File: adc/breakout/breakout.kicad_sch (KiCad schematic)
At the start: 52 parts, among them J1 Conn_01x05_Pin, J2 Conn_01x05_Pin, J3 Conn_01x03_Pin, J4 Conn_01x06_Pin, U1 ESD5344D-TP, U2 ADS1261IRHBR, U3 ESD5344D-TP, U4 ESD5344D-TP

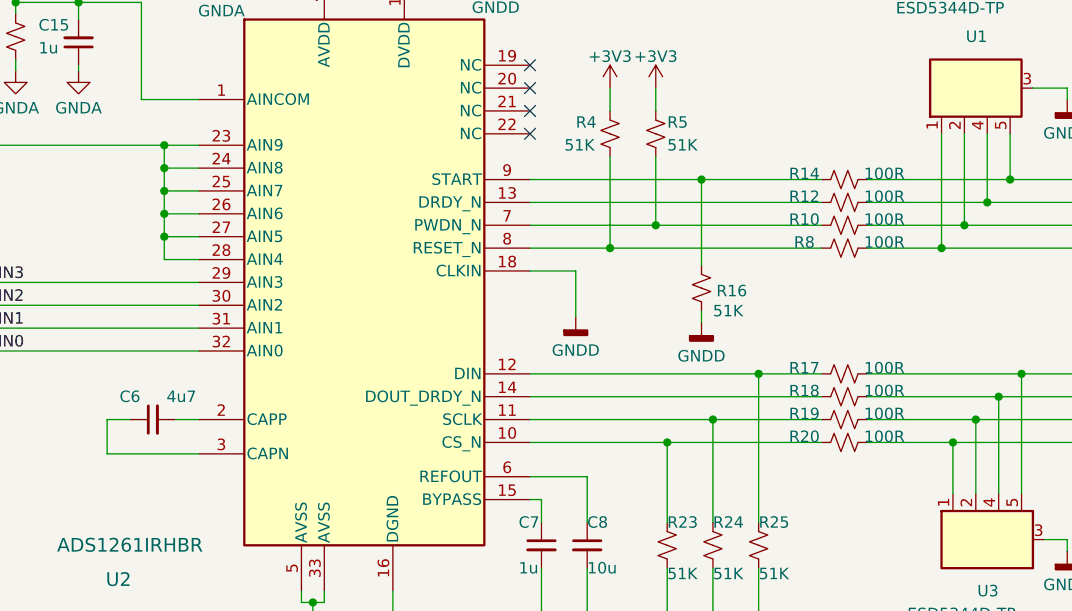
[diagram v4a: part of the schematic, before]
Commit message: Fixed two component values.
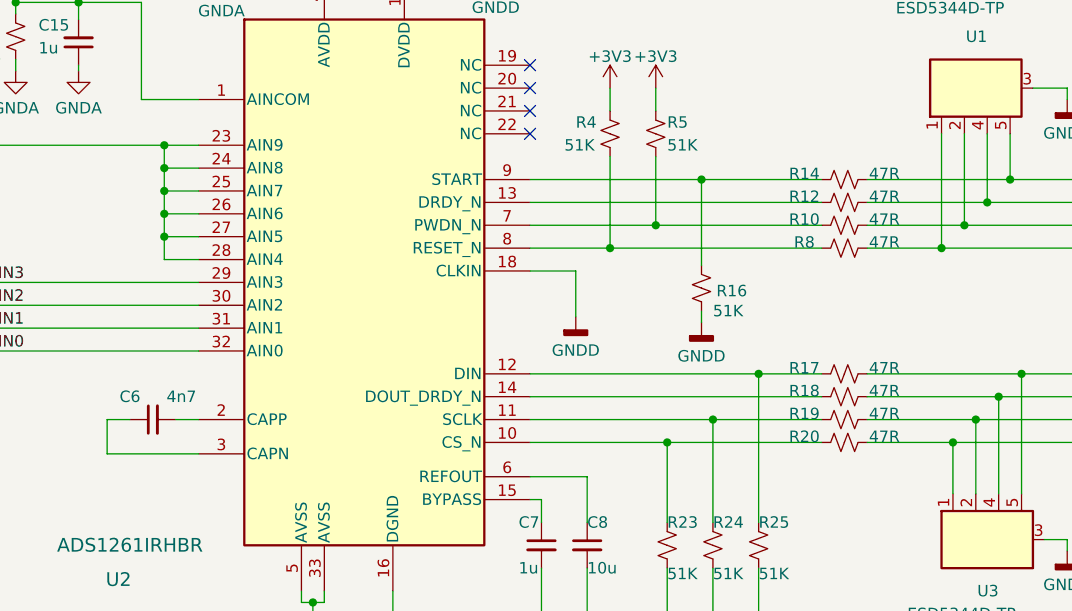
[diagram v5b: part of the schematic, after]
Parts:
- C6: value 4u7 -> 4n7; LCSC C23733 -> C1538
- R10, R12, R14, R17, R18, R19, R20, R8: value 100R -> 47R; LCSC C25076 -> C25118
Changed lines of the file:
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@@
       (effects (font (size 1.27 1.27)))
     )
-    (property "Value" "100R" (at 153.67 75.565 90)
+    (property "Value" "47R" (at 153.67 75.565 90)
       (effects (font (size 1.27 1.27)))
     )
@@
       (effects (font (size 1.27 1.27)) hide)
     )
-    (property "LCSC" "C25076" (at 149.225 76.2 0)
+    (property "LCSC" "C25118" (at 149.225 76.2 0)
       (effects (font (size 1.27 1.27)) hide)
     )
@@
       (effects (font (size 1.27 1.27)))
     )
-    (property "Value" "100R" (at 153.67 73.025 90)
+    (property "Value" "47R" (at 153.67 73.025 90)
       (effects (font (size 1.27 1.27)))
     )
@@
       (effects (font (size 1.27 1.27)) hide)
     )
-    (property "LCSC" "C25076" (at 149.225 73.66 0)
+    (property "LCSC" "C25118" (at 149.225 73.66 0)
       (effects (font (size 1.27 1.27)) hide)
     )
@@
       (effects (font (size 1.27 1.27)))
     )
-    (property "Value" "100R" (at 153.67 89.535 90)
+    (property "Value" "47R" (at 153.67 89.535 90)
       (effects (font (size 1.27 1.27)))
     )
@@
       (effects (font (size 1.27 1.27)) hide)
     )
-    (property "LCSC" "C25076" (at 149.225 90.17 0)
+    (property "LCSC" "C25118" (at 149.225 90.17 0)
       (effects (font (size 1.27 1.27)) hide)
     )
@@
       (effects (font (size 1.27 1.27)))
     )
-    (property "Value" "4u7" (at 75.565 92.71 90)
+    (property "Value" "4n7" (at 75.565 92.71 90)
       (effects (font (size 1.27 1.27)))
     )
@@
       (effects (font (size 1.27 1.27)) hide)
     )
-    (property "LCSC" "C23733" (at 72.39 95.25 0)
+    (property "LCSC" "C1538" (at 72.39 95.25 0)
       (effects (font (size 1.27 1.27)) hide)
     )
@@
       (effects (font (size 1.27 1.27)))
     )
-    (property "Value" "100R" (at 153.67 70.485 90)
+    (property "Value" "47R" (at 153.67 70.485 90)
       (effects (font (size 1.27 1.27)))
     )
@@
       (effects (font (size 1.27 1.27)) hide)
     )
-    (property "LCSC" "C25076" (at 149.225 71.12 0)
+    (property "LCSC" "C25118" (at 149.225 71.12 0)
       (effects (font (size 1.27 1.27)) hide)
     )
@@
       (effects (font (size 1.27 1.27)))
     )
-    (property "Value" "100R" (at 153.67 92.075 90)
+    (property "Value" "47R" (at 153.67 92.075 90)
       (effects (font (size 1.27 1.27)))
     )
@@
       (effects (font (size 1.27 1.27)) hide)
     )
-    (property "LCSC" "C25076" (at 149.225 92.71 0)
+    (property "LCSC" "C25118" (at 149.225 92.71 0)
       (effects (font (size 1.27 1.27)) hide)
     )
@@
       (effects (font (size 1.27 1.27)))
     )
-    (property "Value" "100R" (at 153.67 67.945 90)
+    (property "Value" "47R" (at 153.67 67.945 90)
       (effects (font (size 1.27 1.27)))
     )
@@
       (effects (font (size 1.27 1.27)) hide)
     )
-    (property "LCSC" "C25076" (at 149.225 68.58 0)
+    (property "LCSC" "C25118" (at 149.225 68.58 0)
       (effects (font (size 1.27 1.27)) hide)
     )
@@
       (effects (font (size 1.27 1.27)))
     )
-    (property "Value" "100R" (at 153.67 97.155 90)
+    (property "Value" "47R" (at 153.67 97.155 90)
       (effects (font (size 1.27 1.27)))
     )
@@
       (effects (font (size 1.27 1.27)) hide)
     )
-    (property "LCSC" "C25076" (at 149.225 97.79 0)
+    (property "LCSC" "C25118" (at 149.225 97.79 0)
       (effects (font (size 1.27 1.27)) hide)
     )
@@
       (effects (font (size 1.27 1.27)))
     )
-    (property "Value" "100R" (at 153.67 94.615 90)
+    (property "Value" "47R" (at 153.67 94.615 90)
       (effects (font (size 1.27 1.27)))
     )
@@
       (effects (font (size 1.27 1.27)) hide)
     )
-    (property "LCSC" "C25076" (at 149.225 95.25 0)
-      (effects (font (size 1.27 1.27)) hide)
-    )
+    (property "LCSC" "C25118" (at 149.225 95.25 0)
+      (effects (font (size 1.27 1.27)) hide)
+    )

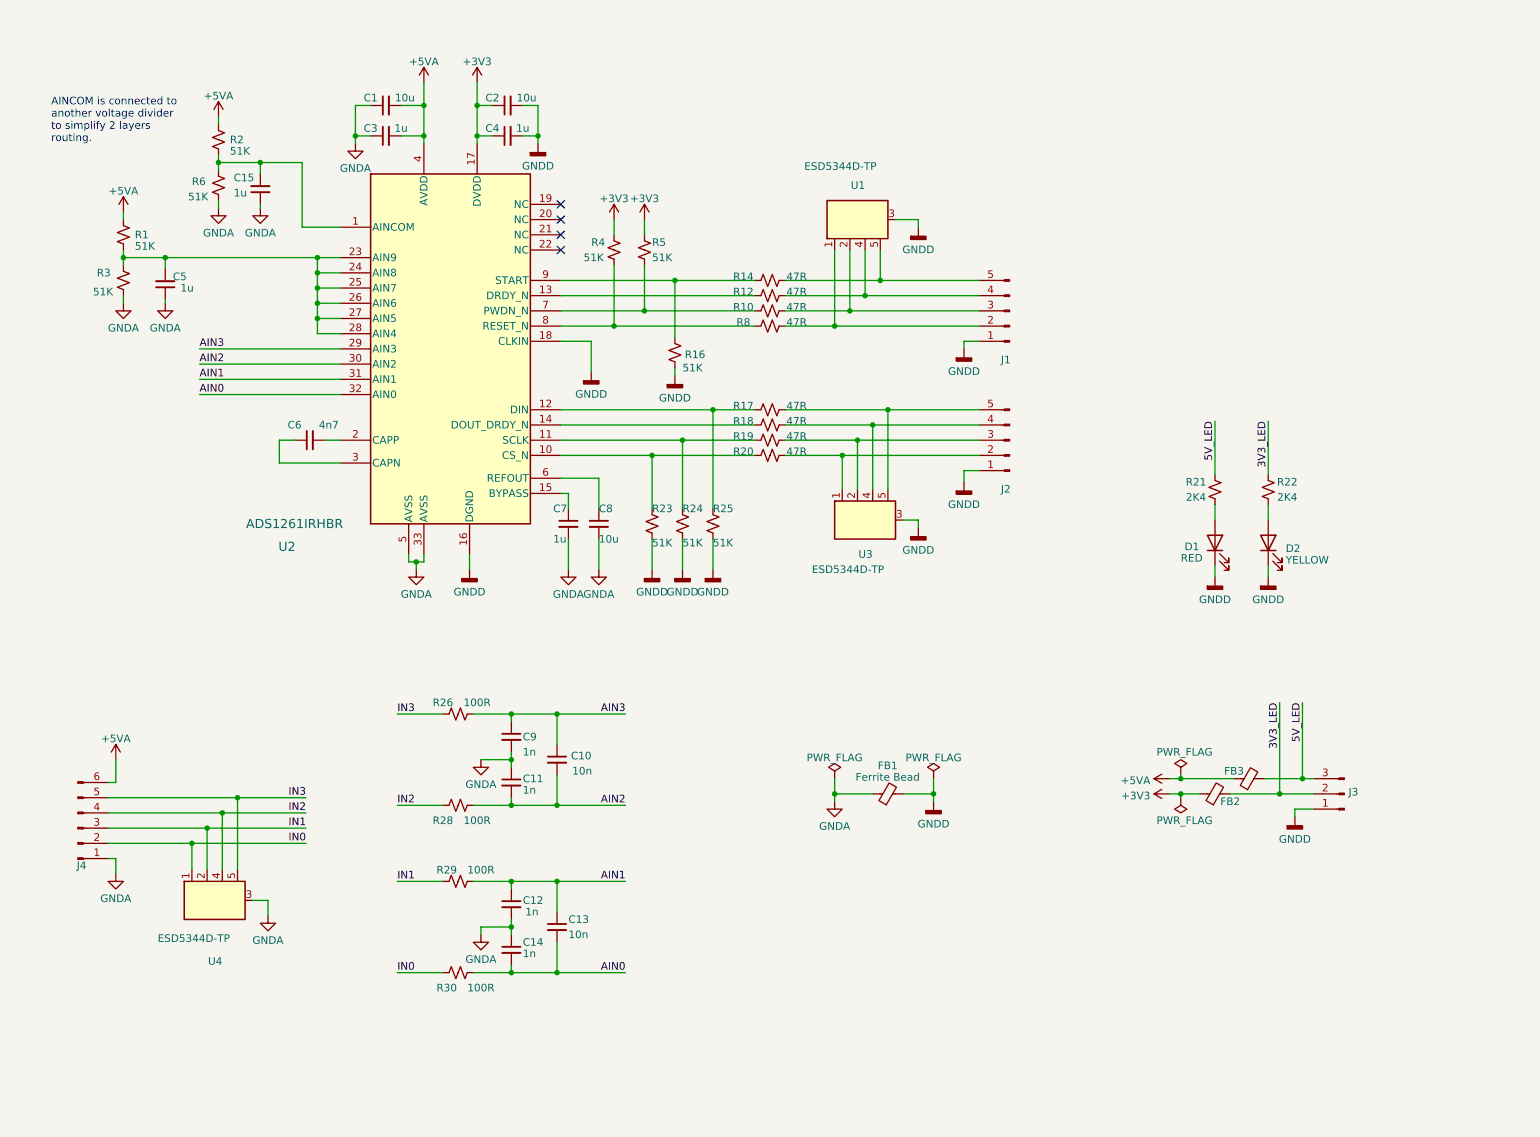
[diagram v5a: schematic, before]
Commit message: Completed the layout of the power supplies.
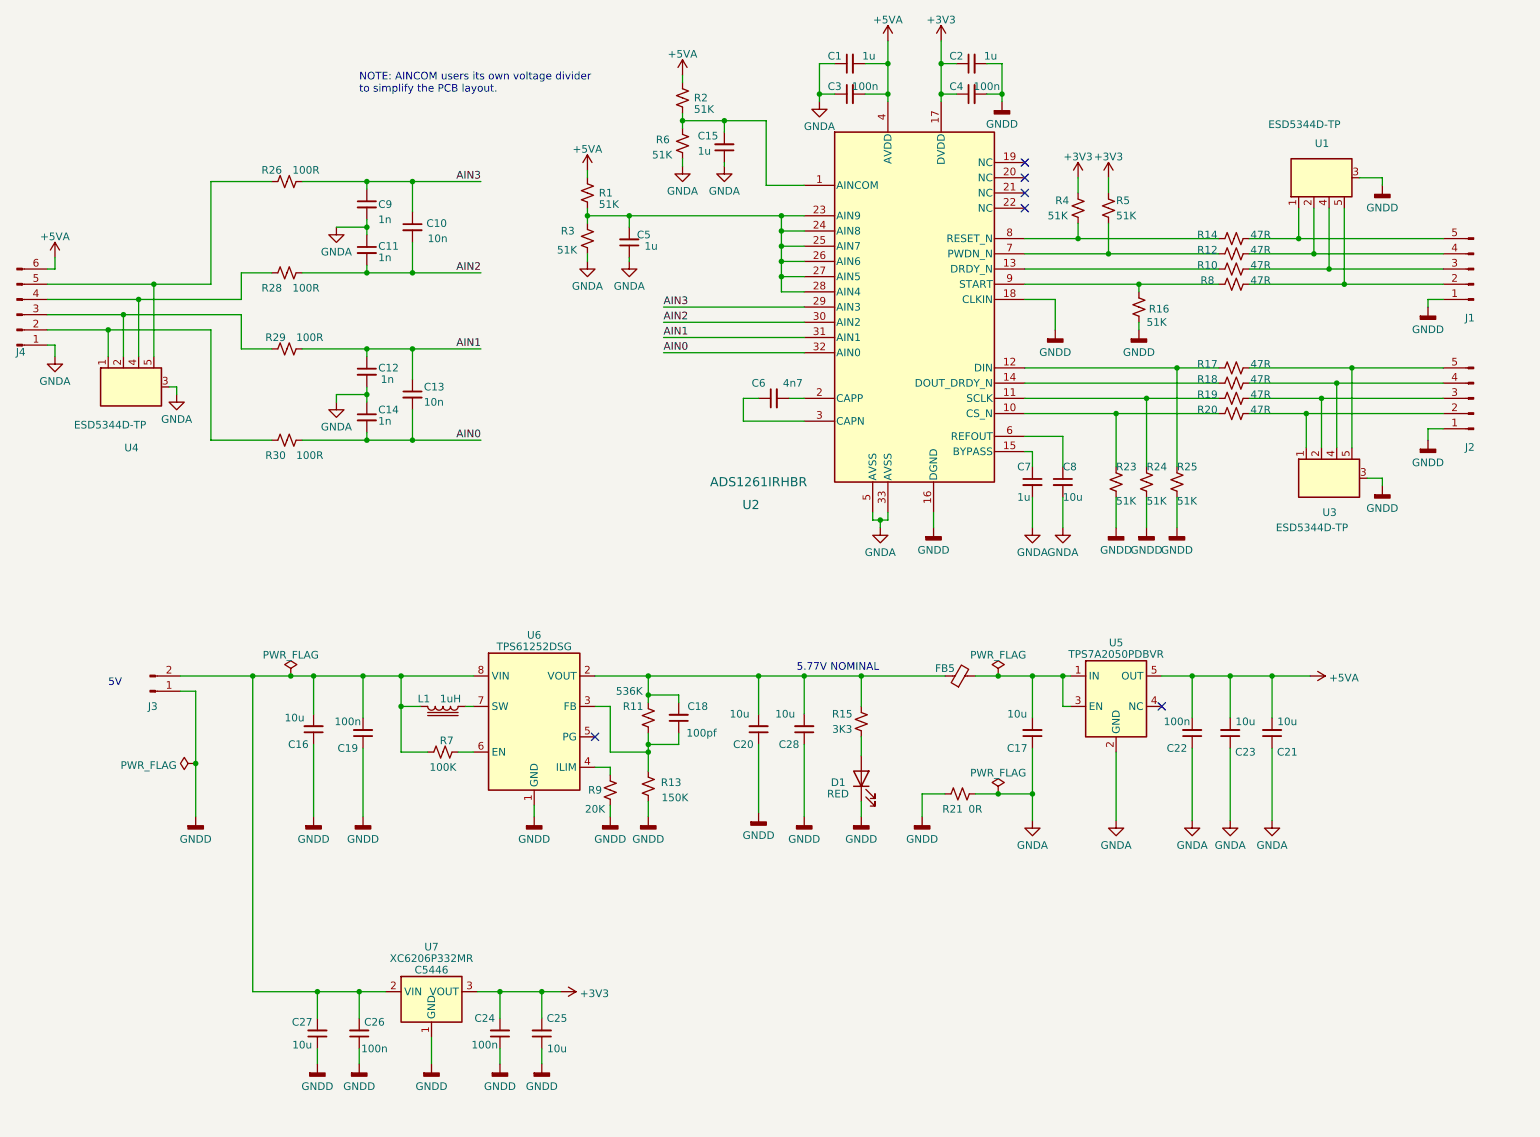
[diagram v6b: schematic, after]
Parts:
- removed D2: YELLOW, LED_SMD:LED_0805_2012Metric, symbol Device:LED
- removed FB1, FB2, FB3: Ferrite Bead, Inductor_SMD:L_0805_2012Metric, symbol Device:FerriteBead_Small
- removed R22: 2K4, Resistor_SMD:R_0402_1005Metric, symbol Device:R_Small_US
- added C16, C17, C20, C21, C23, C25, C27, C28: 10u, Capacitor_SMD:C_0603_1608Metric, symbol Device:C_Small
- added C18: 100pf, Capacitor_SMD:C_0402_1005Metric, symbol Device:C_Small
- added C19, C22, C24, C26: 100n, Capacitor_SMD:C_0402_1005Metric, symbol Device:C_Small
- added FB5: Ferrite Bead, Inductor_SMD:L_0805_2012Metric, symbol Device:FerriteBead_Small
- added L1: 1uH, Inductor_SMD:L_1210_3225Metric, symbol Device:L_Iron
- added R11: 536K, Resistor_SMD:R_0402_1005Metric, symbol Device:R_Small_US
- added R13: 150K, Resistor_SMD:R_0402_1005Metric, symbol Device:R_Small_US
- added R15: 3K3, Resistor_SMD:R_0402_1005Metric, symbol Device:R_Small_US
- added R7: 100K, Resistor_SMD:R_0402_1005Metric, symbol Device:R_Small_US
- added R9: 20K, Resistor_SMD:R_0402_1005Metric, symbol Device:R_Small_US
- added U5: TPS7A2050PDBVR, Package_TO_SOT_SMD:SOT-23-5, symbol breakout:TPS7A2050
- added U6: TPS61252DSG, Package_SON:WSON-8-1EP_2x2mm_P0.5mm_EP0.9x1.6mm, symbol breakout:TPS61252DSG
- added U7: XC6206P332MR, Package_TO_SOT_SMD:SOT-23-3, symbol ble:HT75xx-1-SOT89
- C1, C2: value 10u -> 1u; footprint Capacitor_SMD:C_0603_1608Metric -> Capacitor_SMD:C_0402_1005Metric; LCSC C96446 -> C52923
- C3, C4: value 1u -> 100n; LCSC C52923 -> C1525
- J3: footprint breakout:PinHeader_1x03_P2.54mm_Vertical -> breakout:PinHeader_1x02_P2.54mm_Vertical; symbol Connector:Conn_01x03_Pin -> Connector:Conn_01x02_Pin
- R21: value 2K4 -> 0R; footprint Resistor_SMD:R_0402_1005Metric -> Resistor_SMD:R_0805_2012Metric; LCSC C25882 -> C17477
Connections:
- net +3V3: now also C24.2, C25.2, U7.3 (VOUT)
- net +5VA: now also C21.2, C22.2, C23.2, U5.5 (OUT)
- net GNDA: now also R21.2, C17.1, C21.1, C22.1, C23.1, U5.2 (GND)
- net GNDD: now also R21.1, C16.1, C19.1, C20.1, C24.1, C25.1, C26.1, C27.1, C28.1, R13.2, R9.2, U6.1 (GND), U6.9 (GND), U7.1 (GND)
- net at J1.2 (Pin_2), R8.1: now also U1.5 (D4); no longer U1.1 (D1)
- net at R4.1, U2.8 (RESET_N): now also R14.2; no longer R8.2
- net at J1.3 (Pin_3), R10.1: now also U1.4 (D3); no longer U1.2 (D2)
- net at R5.1, U2.7 (PWDN_N): now also R12.2; no longer R10.2
- net at R16.2, U2.9 (START): now also R8.2; no longer R14.2
- net at U2.13 (DRDY_N): now also R10.2; no longer R12.2
- net at D1.2 (A): now also R15.2; no longer R21.2
- net at J1.4 (Pin_4), R12.1: now also U1.2 (D2); no longer U1.4 (D3)
- net at J1.5 (Pin_5), R14.1: now also U1.1 (D1); no longer U1.5 (D4)
- net 3V3_LED: no longer names the net of J3.2 (Pin_2)
- net 3V3_LED: now also C16.2, C19.2, C26.2, C27.2, L1.1, R7.2, U6.8 (VIN), U7.2 (VIN)
- removed net 5V_LED: J3.3 (Pin_3), R21.1
- net IN0: no longer names the net of J4.2 (Pin_2), R30.1, U4.1 (D1)
- net IN1: no longer names the net of J4.3 (Pin_3), R29.1, U4.2 (D2)
- net IN2: no longer names the net of J4.4 (Pin_4), R28.1, U4.4 (D3)
- net IN3: no longer names the net of J4.5 (Pin_5), R26.1, U4.5 (D4)
- new net: C17.2, FB5.2, U5.1 (IN), U5.3 (EN)
- new net: C18.2, C20.2, C28.2, FB5.1, R11.1, R15.1, U6.2 (VOUT)
- new net: C18.1, R11.2, R13.1, U6.3 (FB)
- new net: R9.1, U6.4 (ILIM)
- new net: L1.2, U6.7 (SW)
- new net: R7.1, U6.6 (EN)
- no-connect marks 4 -> 6
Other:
- note added: "5.77V NOMINAL"
- note added: "5V"
- note added: "NOTE: AINCOM users its own voltage divider to simplify the PCB layout."
- note removed: "AINCOM is connected to another voltage divider to simplify 2 layers routing."
- moved on the sheet: C1, C10, C11, C12, C13, C14, C15, C2, C3, C4, C5, C6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

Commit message: Minor tweaks of the silkscreen layer.
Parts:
- U5: footprint Package_TO_SOT_SMD:SOT-23-5 -> breakout:SOT-23-5
- U6: footprint Package_SON:WSON-8-1EP_2x2mm_P0.5mm_EP0.9x1.6mm -> breakout:WSON-8-1EP_2x2mm_P0.5mm_EP0.9x1.6mm; JLCPCB Rotation Offset (none) -> -90
- U7: JLCPCB Rotation Offset (none) -> -180
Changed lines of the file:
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@@
       (effects (font (size 1.27 1.27)))
     )
-    (property "Footprint" "Package_TO_SOT_SMD:SOT-23-5" (at 212.09 146.05 0)
+    (property "Footprint" "breakout:SOT-23-5" (at 212.09 146.05 0)
       (effects (font (size 1.27 1.27)) hide)
     )
@@
       (effects (font (size 1.27 1.27)))
     )
+    (property "JLCPCB Rotation Offset" "-180" (at 92.71 189.865 0)
+      (effects (font (size 1.27 1.27)) hide)
+    )
     (pin "1")
     (pin "2")
@@
       (effects (font (size 1.27 1.27)))
     )
-    (property "Footprint" "Package_SON:WSON-8-1EP_2x2mm_P0.5mm_EP0.9x1.6mm" (at 111.125 167.64 0)
+    (property "Footprint" "breakout:WSON-8-1EP_2x2mm_P0.5mm_EP0.9x1.6mm" (at 111.125 167.64 0)
       (effects (font (size 1.27 1.27)) hide)
     )
@@
       (effects (font (size 1.27 1.27)) hide)
     )
+    (property "JLCPCB Rotation Offset" "-90" (at 109.855 144.78 0)
+      (effects (font (size 1.27 1.27)) hide)
+    )
